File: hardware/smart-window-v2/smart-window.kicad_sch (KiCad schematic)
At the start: 57 parts, among them J1 Screw_Terminal_01x02, J10 Conn_01x06_Pin, J11 Conn_02x03_Odd_Even, J12 Conn_01x04_Socket, J13 Conn_01x04_Socket, J14 Conn_01x05_Pin, J15 Conn_01x03_Socket, J2 12V INPUT, J3 Screw_Terminal_01x02, J4 Conn_01x03_Socket, J5 Conn_01x03_Socket, J6 Screw_Terminal_01x02, J7 Conn_01x04_Socket, J8 Conn_01x04_Socket, J9 Conn_01x04_Socket, SW1 SW_Push_Dual, SW2 SW_Push_Dual, U1 TSDP341xx, U2 DHT11, U3 L7805, U4 ATmega328P-P, Y1 16MHz

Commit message: Schematic Completed
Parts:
- removed D3: 1N47xxA, Diode_THT:D_DO-41_SOD81_P10.16mm_Horizontal, symbol Diode:1N47xxA
- removed J1: Screw_Terminal_01x02, TerminalBlock:TerminalBlock_bornier-2_P5.08mm, symbol Connector:Screw_Terminal_01x02
- removed PS1: HLK-5M05, Converter_ACDC:Converter_ACDC_Hi-Link_HLK-5Mxx, symbol Converter_ACDC:HLK-5M05
- added FID1, FID2, FID3: Fiducial, Fiducial:Fiducial_1mm_Mask2mm, symbol Mechanical:Fiducial
- added H1, H2, H3, H4: MountingHole, MountingHole:MountingHole_4.3mm_M4, symbol Mechanical:MountingHole
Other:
- note added: "FIDUCIALS"
- note added: "MOUNTING HOLES (M4)"
- note added: "The optimum size of a fiducial marker should be 1 mm. JLC PCB"
- note added: "USER BUTTON"
- note removed: "AC/DC Converter"
- moved on the sheet: C16, D6, R1, SW2

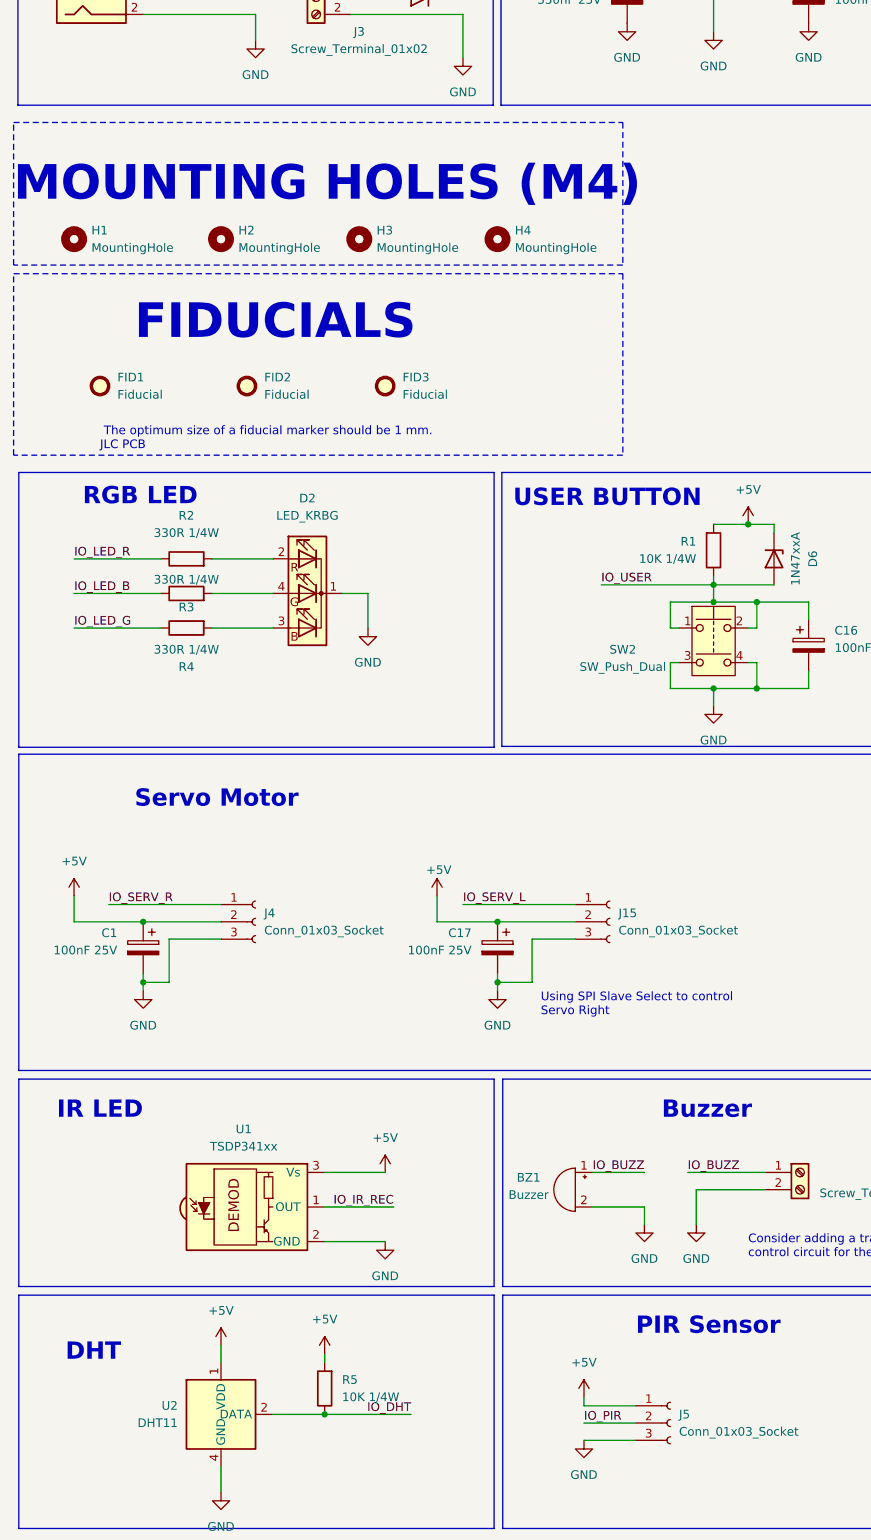
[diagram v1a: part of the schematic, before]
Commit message: Draft of PCB Arragement Complete
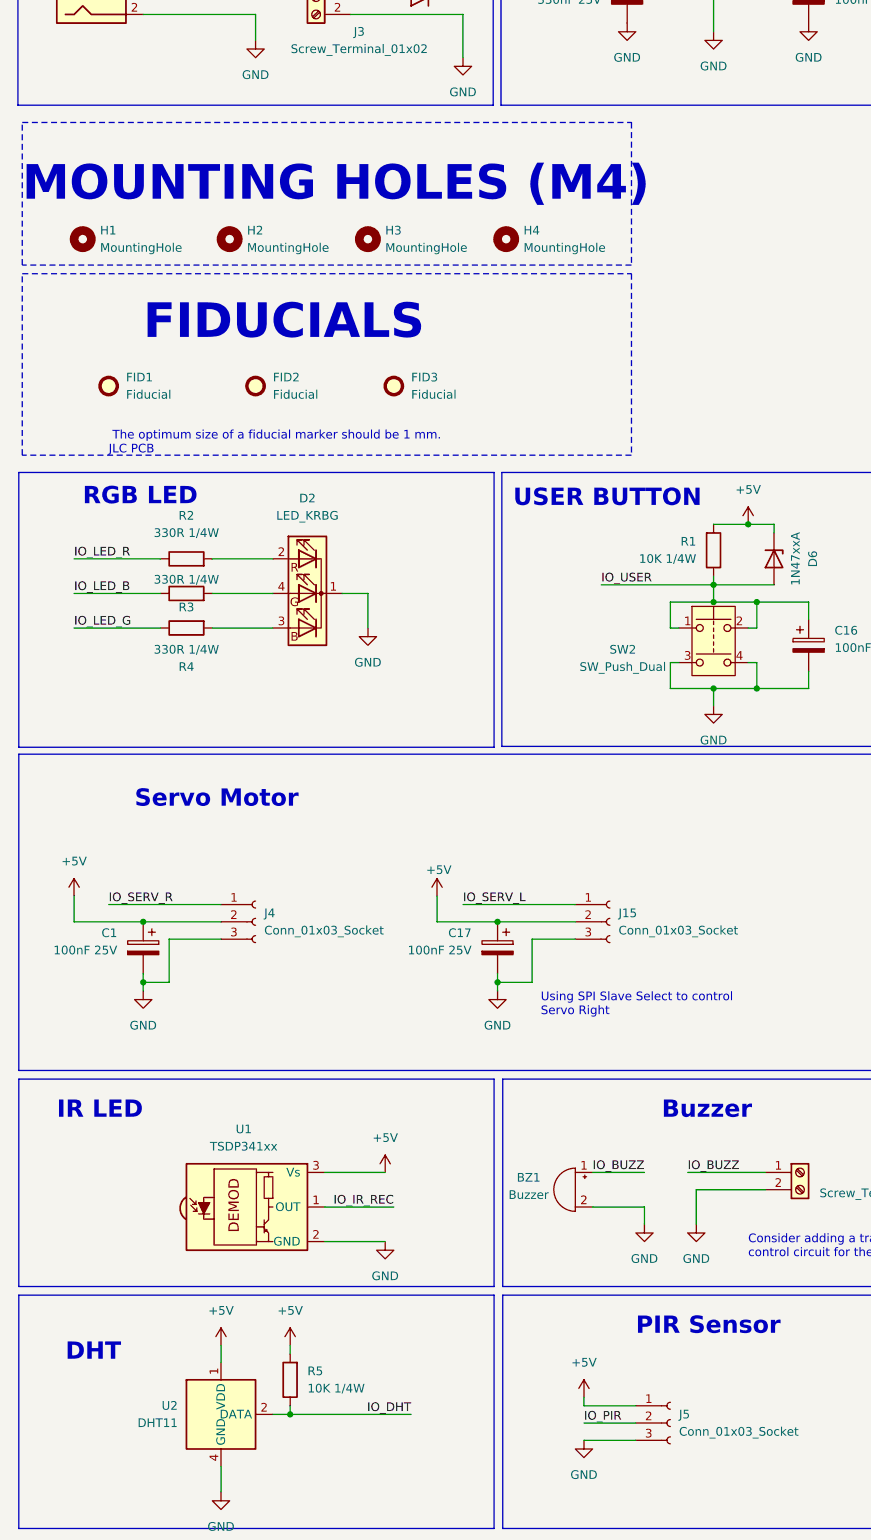
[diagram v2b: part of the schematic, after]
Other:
- moved on the sheet: FID1, FID2, FID3, H1, H2, H3, H4, R5

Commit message: pcb design silkscreen in progress
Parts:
- removed C15, C5, C9: 100nF 25V, Capacitor_THT:CP_Radial_D4.0mm_P2.00mm, symbol Device:C_Polarized
- removed D1: 1N47xxA, Diode_THT:D_DO-41_SOD81_P10.16mm_Horizontal, symbol Diode:1N47xxA
- removed H4: MountingHole, MountingHole:MountingHole_4.3mm_M4, symbol Mechanical:MountingHole
- removed J10: Conn_01x06_Pin, Connector_JST:JST_XH_B6B-XH-AM_1x06_P2.50mm_Vertical, symbol Connector:Conn_01x06_Pin
- removed J14: Conn_01x05_Pin, Connector_PinHeader_2.54mm:PinHeader_1x05_P2.54mm_Vertical, symbol Connector:Conn_01x05_Pin
- removed J2: 12V INPUT, Connector_BarrelJack:BarrelJack_SwitchcraftConxall_RAPC10U_Horizontal, symbol Connector:Barrel_Jack
- removed J6: Screw_Terminal_01x02, TerminalBlock:TerminalBlock_bornier-2_P5.08mm, symbol Connector:Screw_Terminal_01x02
- removed J8, J9: Conn_01x04_Socket, Connector:FanPinHeader_1x04_P2.54mm_Vertical, symbol Connector:Conn_01x04_Socket
- removed R7, R8, R9: 330R 1/4W, Resistor_THT:R_Axial_DIN0207_L6.3mm_D2.5mm_P15.24mm_Horizontal, symbol Device:R
- removed SW1: SW_Push_Dual, symbol Switch:SW_Push_Dual
- removed SW2: SW_Push_Dual, Button_Switch_THT:SW_PUSH_6mm, symbol Switch:SW_Push_Dual
- added C10: 100nF 25V, Capacitor_THT:CP_Radial_D4.0mm_P2.00mm, symbol Device:C_Polarized
- added J1: Barrel_Jack_MountingPin, Connector_BarrelJack:BarrelJack_Horizontal, symbol Connector:Barrel_Jack_MountingPin
- added J12, J14: Screw_Terminal_01x02, TerminalBlock_Altech:Altech_AK100_1x02_P5.00mm, symbol Connector:Screw_Terminal_01x02
- added J7: Conn_01x04_Socket, Connector:FanPinHeader_1x04_P2.54mm_Vertical, symbol Connector:Conn_01x04_Socket
- added J9: Conn_01x02, Connector_PinSocket_2.54mm:PinSocket_1x02_P2.54mm_Vertical, symbol PCM_4ms_Connector:Conn_01x02
- added JP1, JP2, JP3: SolderJumperOpen, Jumper:SolderJumper-2_P1.3mm_Open_TrianglePad1.0x1.5mm, symbol Jumper:SolderJumper_2_Open
- added SW1, SW2: SW_Push, Button_Switch_THT:SW_PUSH_6mm_H4.3mm, symbol Switch:SW_Push
- added TP1, TP2, TP3, TP4, TP5, TP6: TestPoint, PCM_4ms_TestPoint:TestPoint_Pad_04, symbol Connector:TestPoint
- J2: renamed from J4; footprint Connector:FanPinHeader_1x03_P2.54mm_Vertical -> PCM_4ms_Connector:Pins_1x03_2.54mm_TH
- J3: footprint TerminalBlock:TerminalBlock_bornier-2_P5.08mm -> TerminalBlock_Altech:Altech_AK100_1x02_P5.00mm
- J4: renamed from J15; footprint Connector:FanPinHeader_1x03_P2.54mm_Vertical -> PCM_4ms_Connector:Pins_1x03_2.54mm_TH
- renumbered C10 to C11, C11 to C13, C12 to C14, C13 to C15, C14 to C16, C17 to C2, C2 to C3, C16 to C4, C3 to C5, C4 to C6, C6 to C7, C7 to C8, C8 to C9, D4 to D3, D6 to D4, J12 to J10, J13 to J11, J7 to J6, J11 to J8, R2 to R1, R3 to R2, R4 to R3, R5 to R4, R1 to R5, U2 to U1, U1 to U2
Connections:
- net +5V: now also J11.4 (Pin_4), C10.1, JP1.1 (A), JP2.1 (A), JP3.1 (A), TP2.1; no longer J11.1 (Pin_1), J6.1 (Pin_1)
- net AD3_MQ2: now also J11.1 (Pin_1); no longer J11.4 (Pin_4)
- net AD4/SDA: now also J7.1 (Pin_1), TP5.1
- net AD5/SCL: now also J7.2 (Pin_2), TP6.1
- net AVCC_IND: now also JP2.2 (B)
- net GND: now also J11.3 (Pin_3), J6.1 (Pin_1), C10.2, J1.2, J1.MP (MountPin), J12.1 (Pin_1), J14.2 (Pin_2), J7.4 (Pin_4), J9.2 (Pin_2), SW1.1, SW2.1, TP3.1; no longer J11.2 (Pin_2), J6.4 (Pin_4)
- net IO_LED_B: now also U4.24 (PC1); no longer U4.23 (PC0)
- net IO_LED_G: now also U4.23 (PC0); no longer U4.24 (PC1)
- net IO_SERV_L: now also J12.2 (Pin_2)
- net IO_SERV_R: now also J14.1 (Pin_1)
- net IO_USER: now also SW1.2
- net MCU_RESET: now also SW2.2, TP4.1
- net MCU_RXD: now also J6.2 (Pin_2); no longer J6.3 (Pin_3)
- net MCU_SS: now also J9.1 (Pin_1)
- net MCU_TXD: now also J6.3 (Pin_3); no longer J6.2 (Pin_2)
- net VCC: now also TP1.1
- net +VCC_BARREL: now reaches D3.2 (A), J3.1 (Pin_1)
- net +VCC_BARREL: now also J1.1
- net BLUE_L: now reaches D2.3 (BA), R3.2
- net GREEN_L: now reaches D2.4 (GA), R2.2
- net RED_L: now reaches D2.2 (RA), R1.2
- new net +I2C_JUMP: J7.3 (Pin_3), JP1.2 (B)
- new net +UART_JUMP: J6.4 (Pin_4), JP3.2 (B)
- no-connect marks 4 -> 3
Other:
- note added: "I2C Connector"
- note added: "SPI Slave Select"
- note removed: "I2C Connector's"
- note removed: "SPI Connector"
- note removed: "UART Programming Header"
- note removed: "Using SPI Slave Select to control Servo Right"
- moved on the sheet: BZ1, C1, C15, C16, C2, C4, C5, C6, C9, D2, D3, D4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
